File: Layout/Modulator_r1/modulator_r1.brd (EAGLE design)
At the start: 75.2 x 49.5 mm, 76 parts, among them Q1 FA-20H, U1 ATMEGA328P-AU, U2 TPS79933QDDCRQ1, U3 CC1125RHBT, U4 MCP1700T-3302E/TT, U5 FT232RL, U6 SIP32509DT-T1-GE3

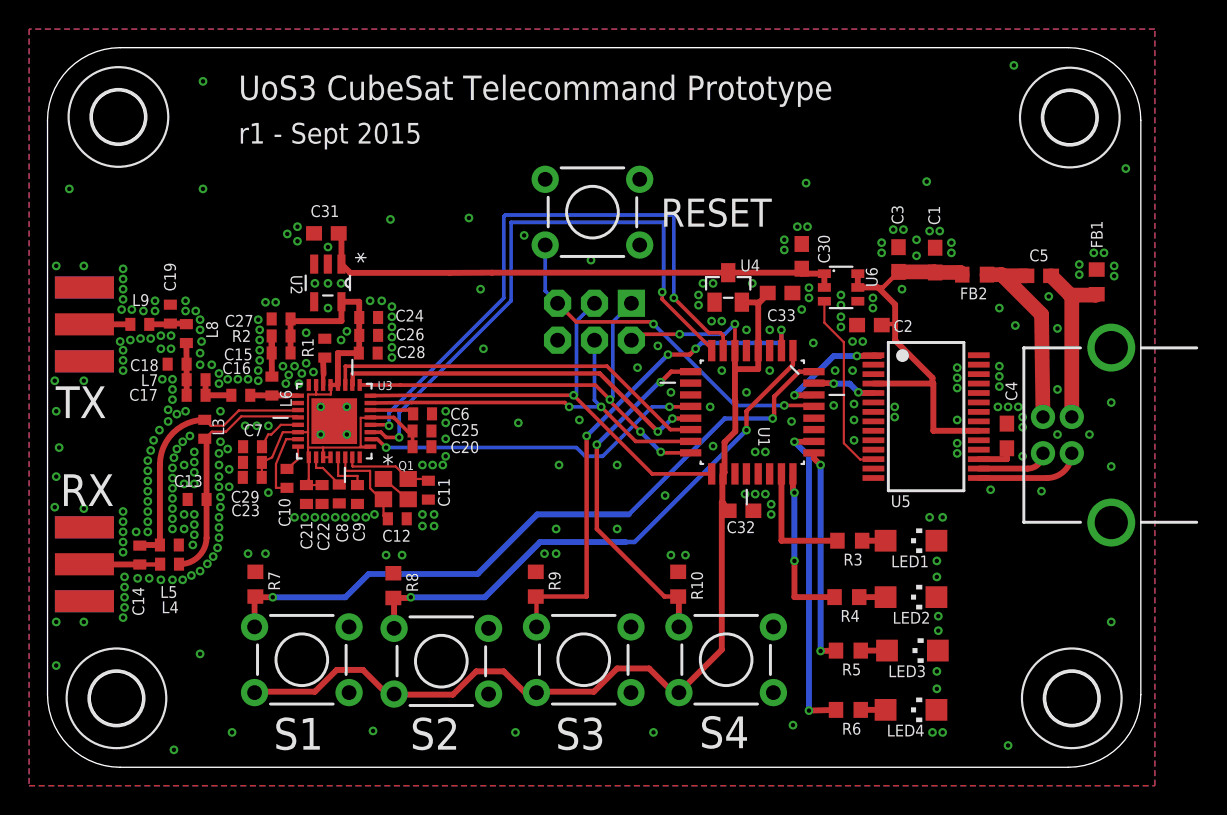
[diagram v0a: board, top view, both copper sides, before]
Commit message: Add test pads.
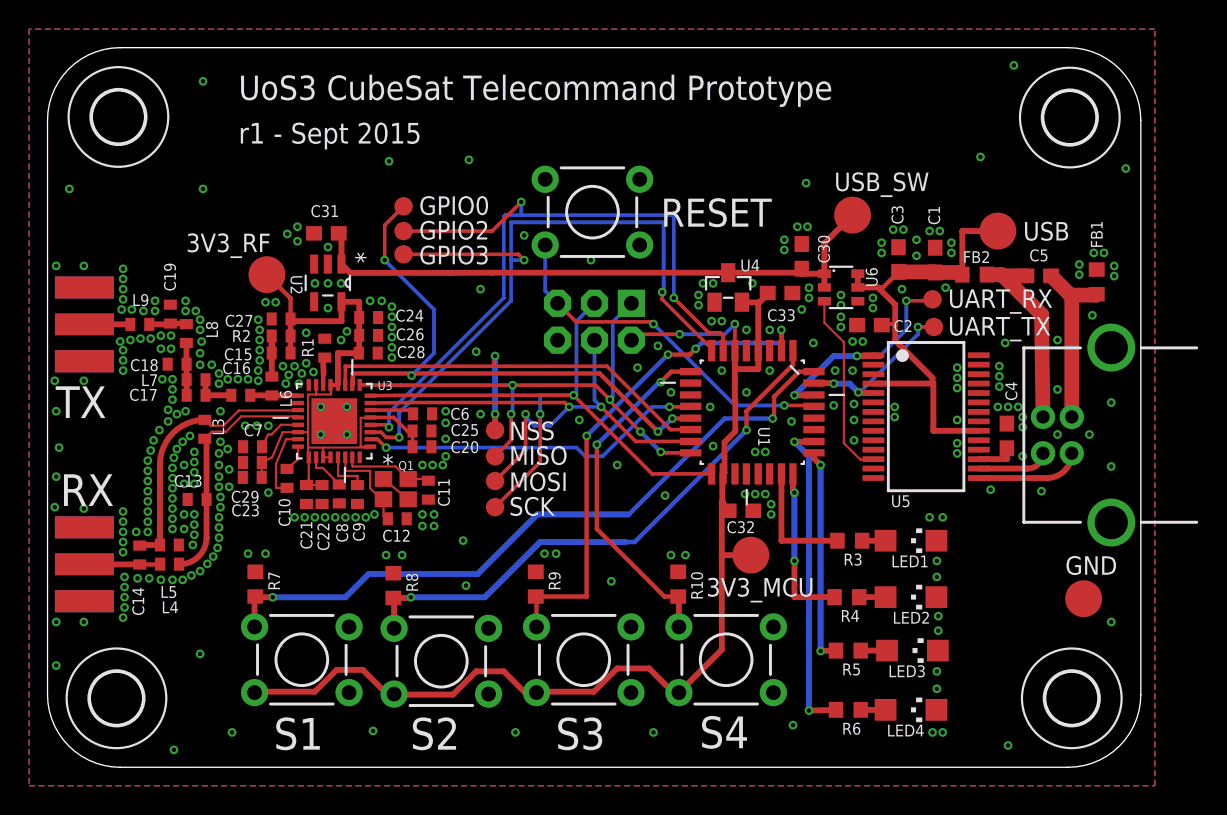
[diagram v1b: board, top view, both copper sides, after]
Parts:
- added 3V3_MCU, 3V3_RF, GND, USB, USB_SW: PTR1B2,54, testpad:B2,54
- added GPIO0, GPIO2, GPIO3, MISO, MOSI, NSS, SCK, UART_RX, UART_TX: PTR1B1,27, testpad:B1,27
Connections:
- net +3V3: now also 3V3_MCU.TP
- net CC_IO0: now also GPIO0.TP
- net CC_IO2: now also GPIO2.TP
- net CC_IO3: now also GPIO3.TP
- net CC_VDD: now also 3V3_RF.TP
- net GND: now also GND.TP
- net MISO: now also MISO.TP
- net MOSI: now also MOSI.TP
- net NSS: now also NSS.TP
- net SCK: now also SCK.TP
- net UART_RX: now also UART_TX.TP
- net UART_TX: now also UART_RX.TP
- net VCCIO: now also USB.TP
- net VCC_LOGIC: now also USB_SW.TP
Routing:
- net CC_IO0: track 26.1 -> 40.5 mm, vias 2 -> 4
- net SCK: track 32.8 -> 44.1 mm, vias 1 -> 2
- net CC_IO2: track 41.9 -> 51.9 mm, vias 2 -> 3
- net MOSI: track 27.9 -> 37.4 mm, vias 2 -> 3
- net CC_IO3: track 40.9 -> 50.3 mm, vias 2 -> 3
- net UART_TX: track 8.80 -> 16.8 mm, vias 2 -> 3
- net UART_RX: track 4.38 -> 11.7 mm, vias 2 -> 3
- net NSS: track 26.9 -> 32.7 mm, vias 0 -> 2
- net VCCIO: track 28.3 -> 33.7 mm
- net MISO: track 32.0 -> 37.4 mm, vias 3 -> 5
- net VCC_LOGIC: track 37.3 -> 42.2 mm
- net CC_VDD: track 47.4 -> 51.1 mm
- net +3V3: track 77.6 -> 79.6 mm

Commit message: Tweak labels.
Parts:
- moved 3V3_MCU 4.16 mm to (44.6, 16.3)
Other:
- board text added: "ICSP"
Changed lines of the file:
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@@
 <text x="62.7" y="2.8" size="2.1844" layer="27">L4</text>
 <text x="13.14" y="42.92" size="1.4224" layer="25" font="vector" ratio="10">r1 - Sept 2015</text>
+<text x="34.9" y="25.5" size="1.9304" layer="25">ICSP</text>
 </plain>
 <attributes>
@@
 <attribute name="TP_SIGNAL_NAME" value="" x="55.4" y="38" size="1.778" layer="27" display="off"/>
 </element>
-<element name="3V3_MCU" library="testpad" package="B2,54" value="PTR1B2,54" x="48.4" y="14.6" smashed="yes">
-<attribute name="TP_SIGNAL_NAME" value="" x="47.13" y="11.425" size="1" layer="37"/>
-<attribute name="NAME" x="45.33" y="11.751" size="1.27" layer="25" ratio="10"/>
-<attribute name="VALUE" x="47.13" y="13.203" size="0.0254" layer="27"/>
+<element name="3V3_MCU" library="testpad" package="B2,54" value="PTR1B2,54" x="44.6" y="16.3" smashed="yes">
+<attribute name="TP_SIGNAL_NAME" value="" x="43.33" y="13.125" size="1" layer="37"/>
+<attribute name="NAME" x="37.83" y="17.851" size="1.27" layer="25" ratio="10"/>
+<attribute name="VALUE" x="43.33" y="14.903" size="0.0254" layer="27"/>
 </element>
 <element name="3V3_RF" library="testpad" package="B2,54" value="PTR1B2,54" x="15.1" y="33.9" smashed="yes">
@@
 <via x="45.8" y="22.1" extent="1-16" drill="0.3"/>
 <via x="42.9" y="25.8" extent="1-16" drill="0.3"/>
-<via x="40.6" y="27.5" extent="1-16" drill="0.3"/>
+<via x="40.2" y="27.1" extent="1-16" drill="0.3"/>
 <via x="42" y="29" extent="1-16" drill="0.3"/>
 <via x="39.2" y="20.8" extent="1-16" drill="0.3"/>
-<via x="42.5" y="18.7" extent="1-16" drill="0.3"/>
+<via x="43.3" y="19.4" extent="1-16" drill="0.3"/>
 <via x="38.8" y="12.8" extent="1-16" drill="0.3"/>
 <via x="28.8" y="12.5" extent="1-16" drill="0.3"/>
@@
 <contactref element="S4" pad="3"/>
 <wire x1="46.87" y1="17.65" x2="46.4" y2="18.25" width="0.4064" layer="1"/>
-<wire x1="46.4" y1="18.25" x2="46.4" y2="14.6" width="0.4064" layer="1"/>
-<wire x1="46.4" y1="14.6" x2="46.4" y2="8.0906" width="0.4064" layer="1"/>
+<wire x1="46.4" y1="18.25" x2="46.4" y2="16.3" width="0.4064" layer="1"/>
+<wire x1="46.4" y1="16.3" x2="46.4" y2="8.0906" width="0.4064" layer="1"/>
 <wire x1="46.4" y1="8.0906" x2="43.4488" y2="5.1394" width="0.4064" layer="1"/>
 <wire x1="43.4488" y1="5.1394" x2="43.0606" y2="5.1394" width="0.4064" layer="1"/>
@@
 <via x="47.3" y="30.5" extent="1-16" drill="0.3"/>
 <contactref element="3V3_MCU" pad="TP"/>
-<wire x1="48.4" y1="14.6" x2="46.4" y2="14.6" width="0.4064" layer="1"/>
+<wire x1="44.6" y1="16.3" x2="46.4" y2="16.3" width="0.4064" layer="1"/>
 </signal>
 <signal name="UART_TX">

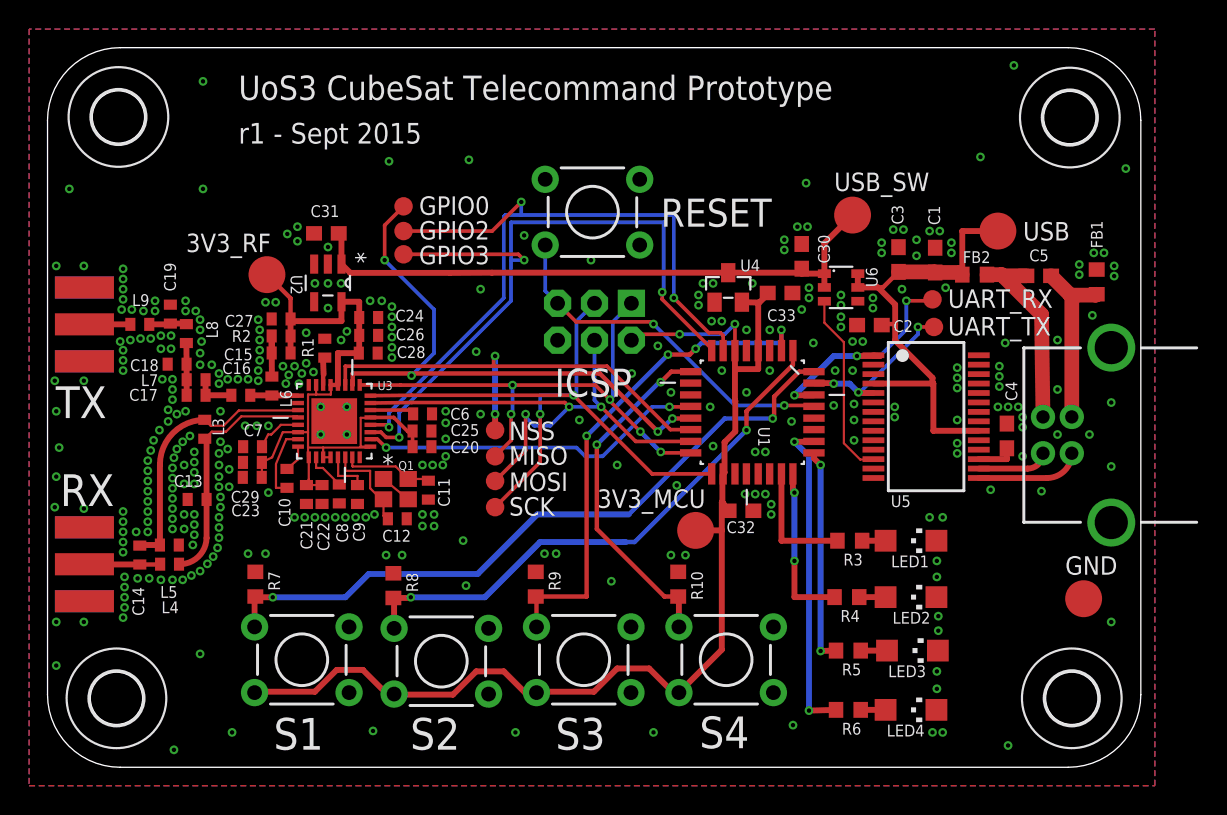
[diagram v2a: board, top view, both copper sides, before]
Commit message: Add UoS3 and SUSF logos. Closes #7.
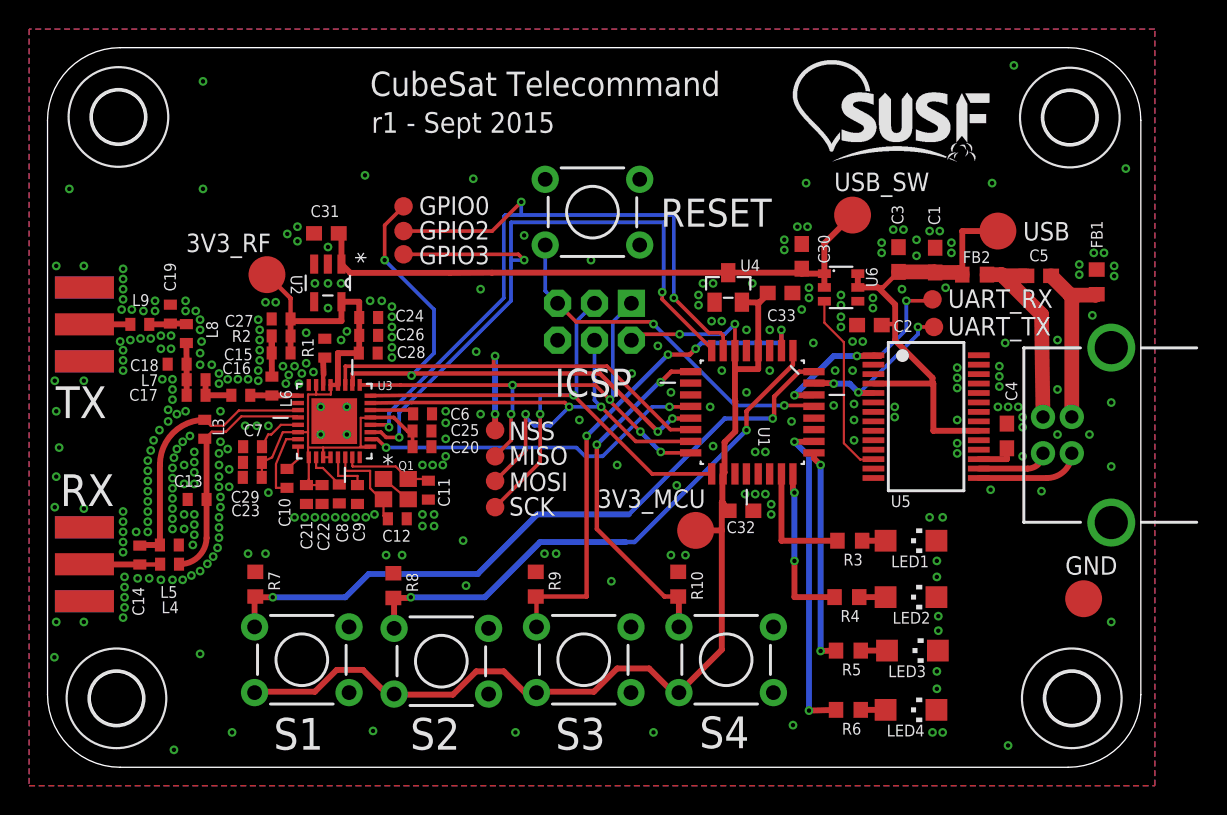
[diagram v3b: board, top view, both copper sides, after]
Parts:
- added U$1: (no value), Mine:SUSF-XSM
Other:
- board text added: "/home/phil/files-philcrump/Cubesat/uos3-pcb.bmp"
- board text added: "CubeSat Telecommand"
- board text removed: "UoS3 CubeSat Telecommand Prototype"

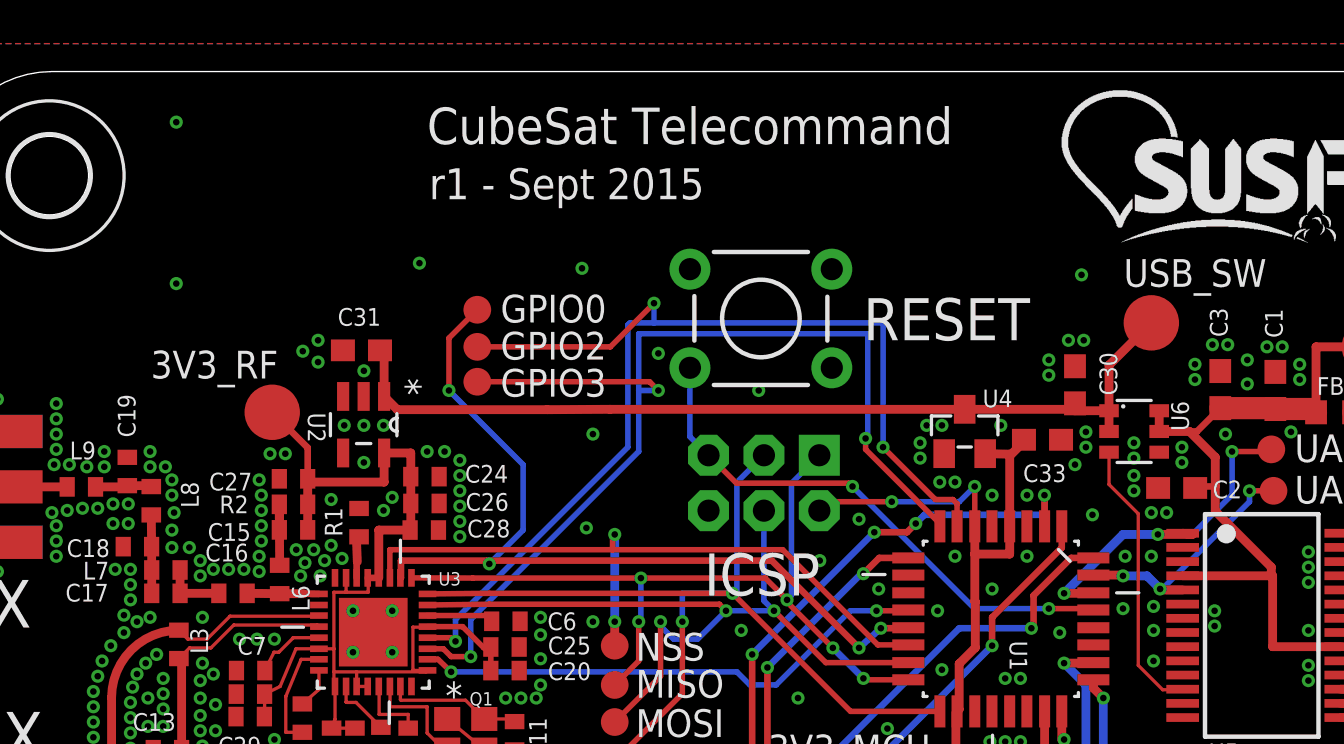
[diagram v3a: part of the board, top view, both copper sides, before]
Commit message: Add DTR coupling to reset. Closes #9.
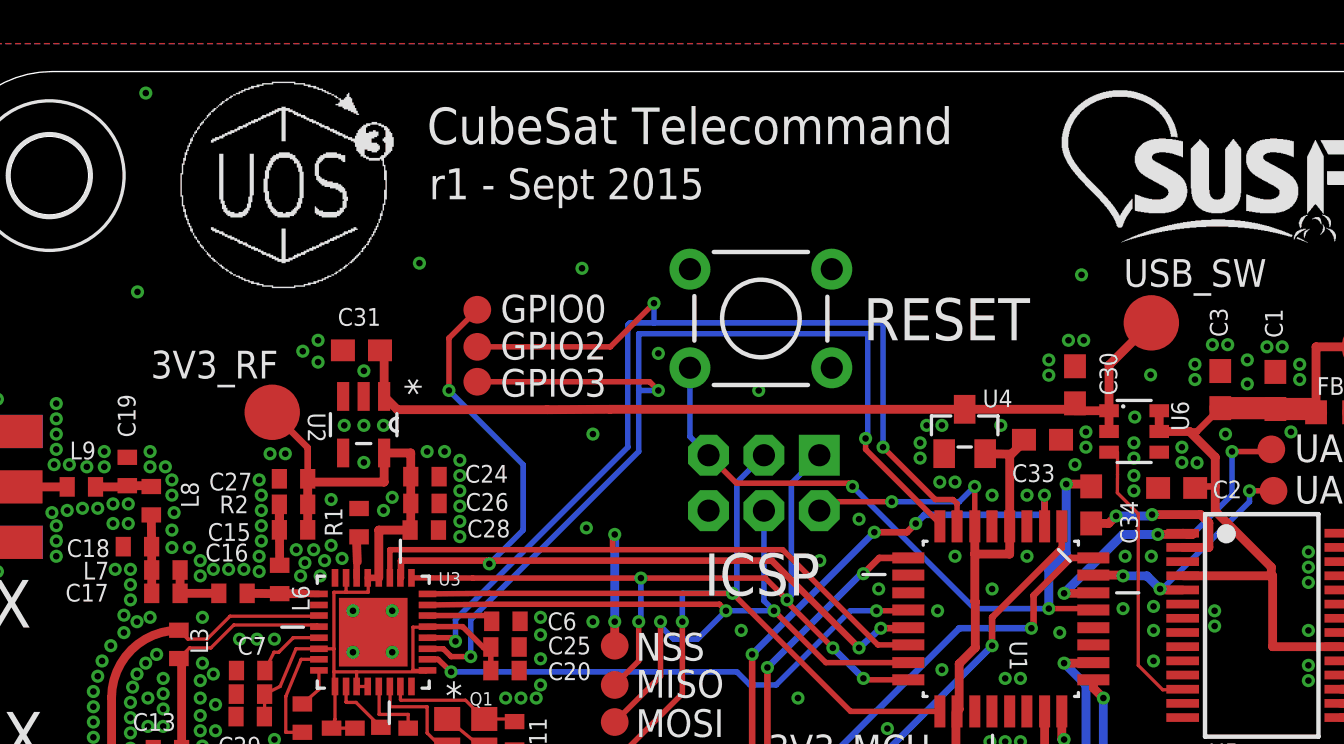
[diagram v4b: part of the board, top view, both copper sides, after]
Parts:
- added C34: 100nF, resistor:C0603
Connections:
- new net N$20: C34.2, U5.2
- net AVR_NRESET: now also C34.1
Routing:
- net N$20: track 0.00 -> 8.05 mm, vias 0 -> 2
- net AVR_NRESET: track 25.0 -> 32.2 mm, vias 2 -> 3

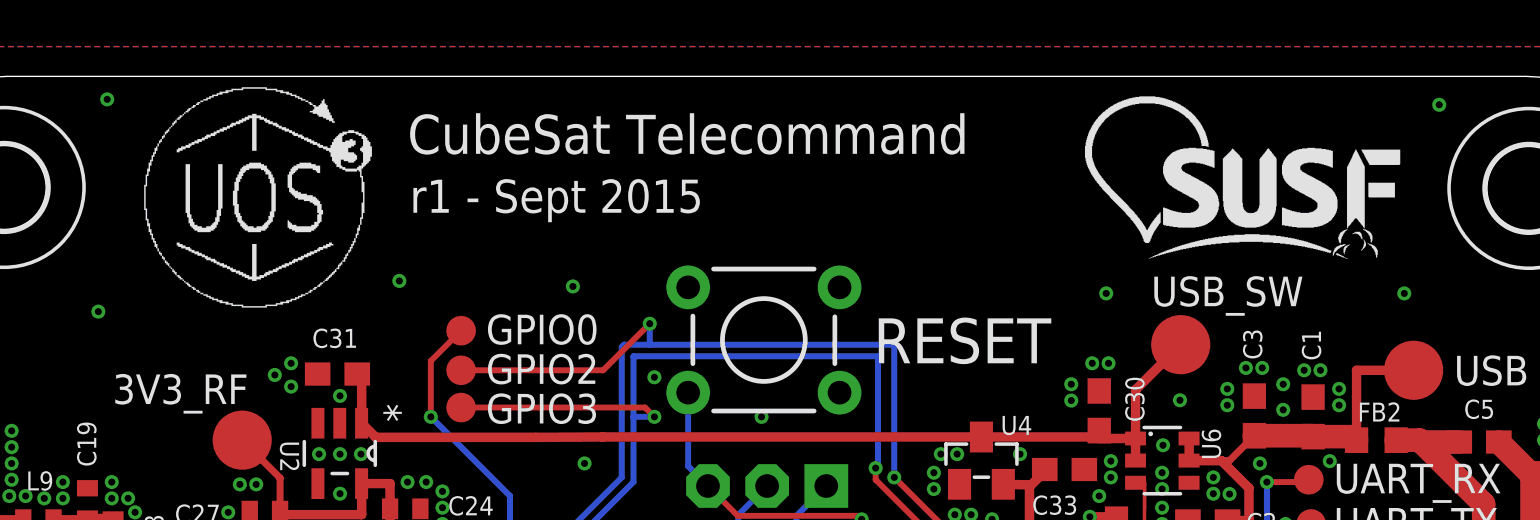
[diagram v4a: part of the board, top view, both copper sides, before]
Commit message: Tweak silkscreen.
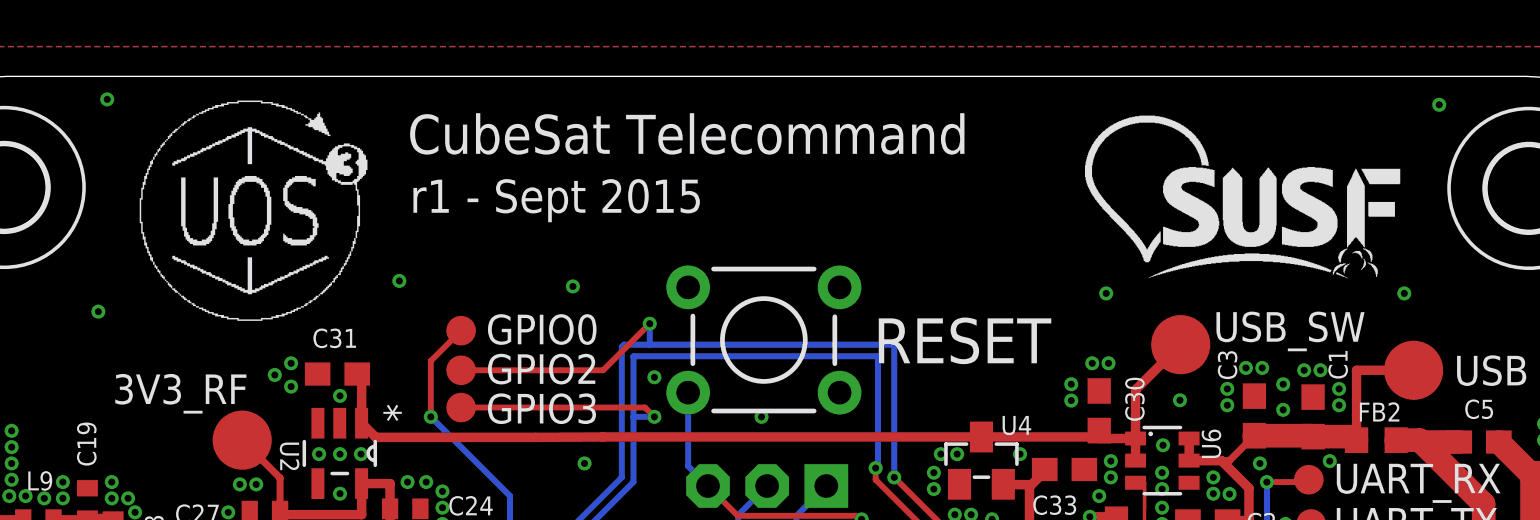
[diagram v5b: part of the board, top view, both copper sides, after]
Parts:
- moved U$1 0.83 mm to (51.3, 40.9)
